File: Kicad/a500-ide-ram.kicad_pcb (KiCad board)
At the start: 2 copper layers, 82.5 x 34.9 mm, 28 parts, among them J1 power, J2 LED, J3 LED2, J4 INT2OVR, J5 INT2, J6 JTAG, J7 IDE, U1 68000D socket, U13 XC6206PxxxMR, U2 XC95144XL-TQ100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

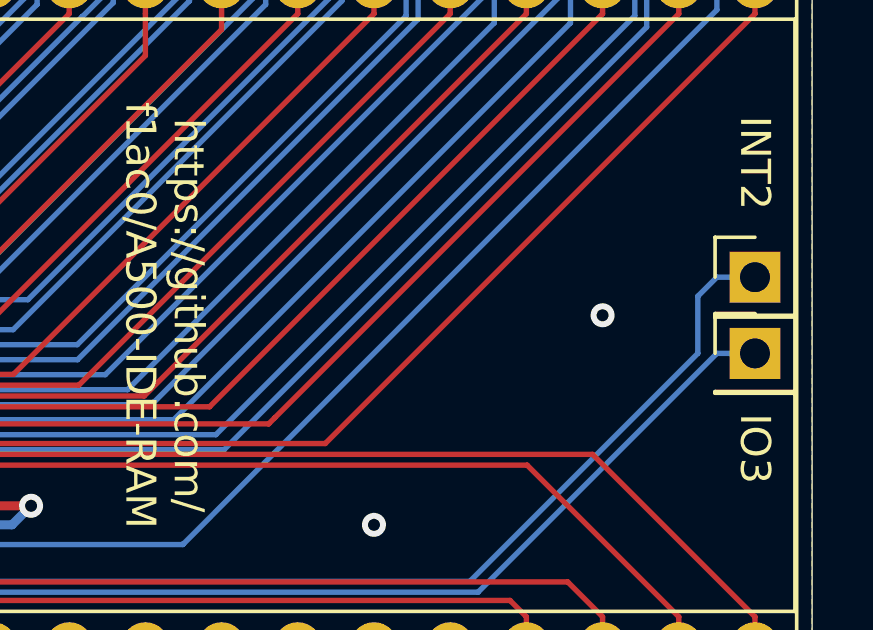
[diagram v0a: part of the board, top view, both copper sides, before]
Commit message: KiCAD : correct license on schematic and PCB
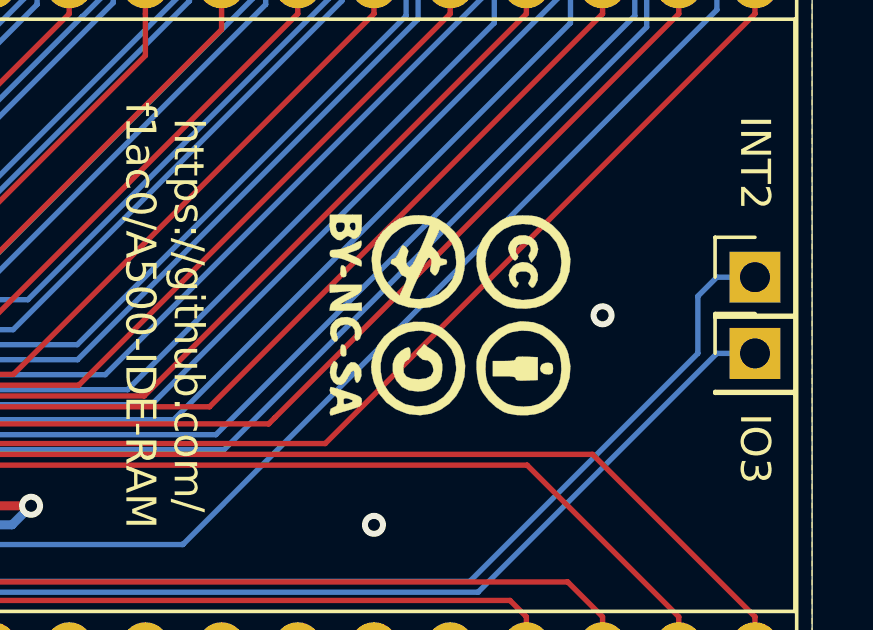
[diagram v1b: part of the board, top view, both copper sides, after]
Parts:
- added FID1: Fiducial, Sassa:CC_BY_NC_SA_square_silkscreen, F.Cu at (174.6, 97.2)
